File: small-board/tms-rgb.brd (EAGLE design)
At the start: 53.1 x 17.6 mm, 38 parts, among them J1 Pads, U1 CD74HC4053PWR, U100 TMS992XA, U2 LM1881MX/NOPB, U3 MAX4395EUD, U4 TS5A4597DCKR, U5 SN74LVC2G17DCKR, U6 LMH1251MT/NOPB, U7 THS7374IPWR

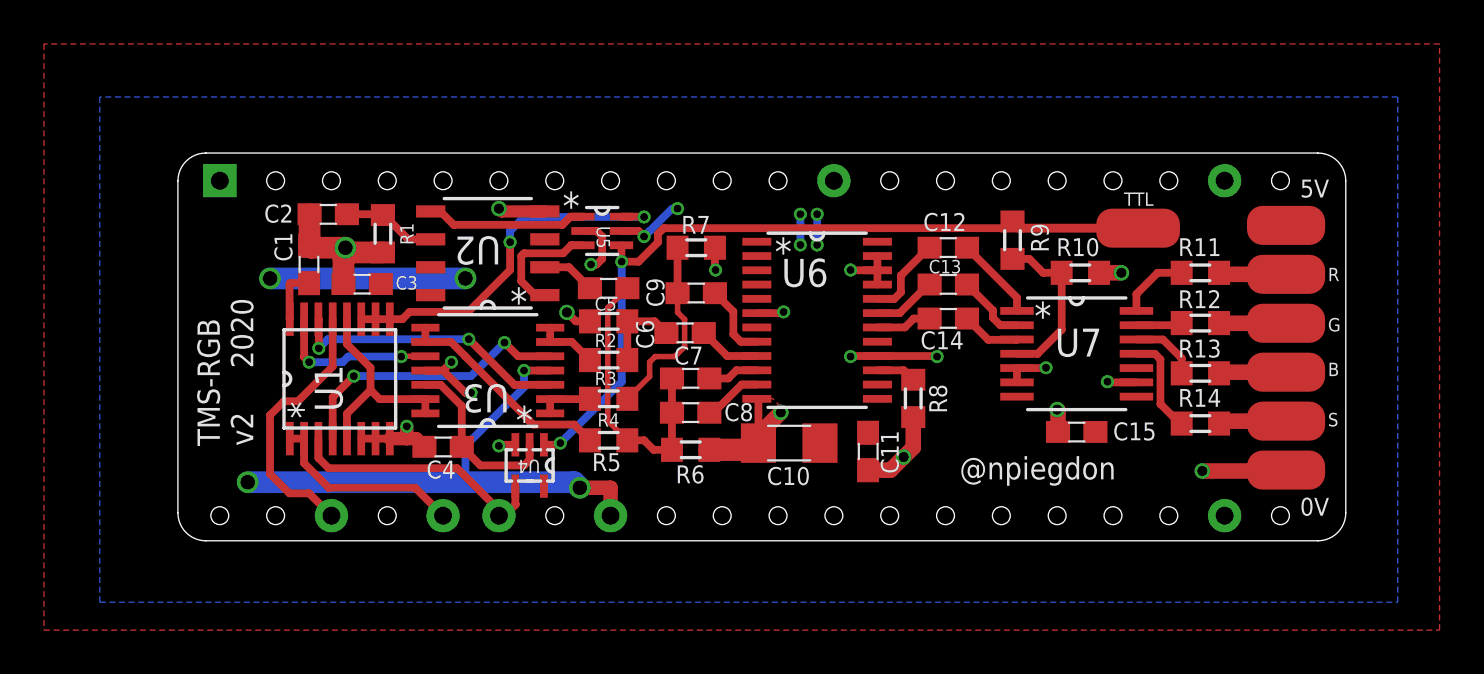
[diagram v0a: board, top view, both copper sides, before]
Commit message: More than 100 improvements
Nearly all of which were suggested by MrPix from the AtariAge forums to improve the electrical characteristics of the board.
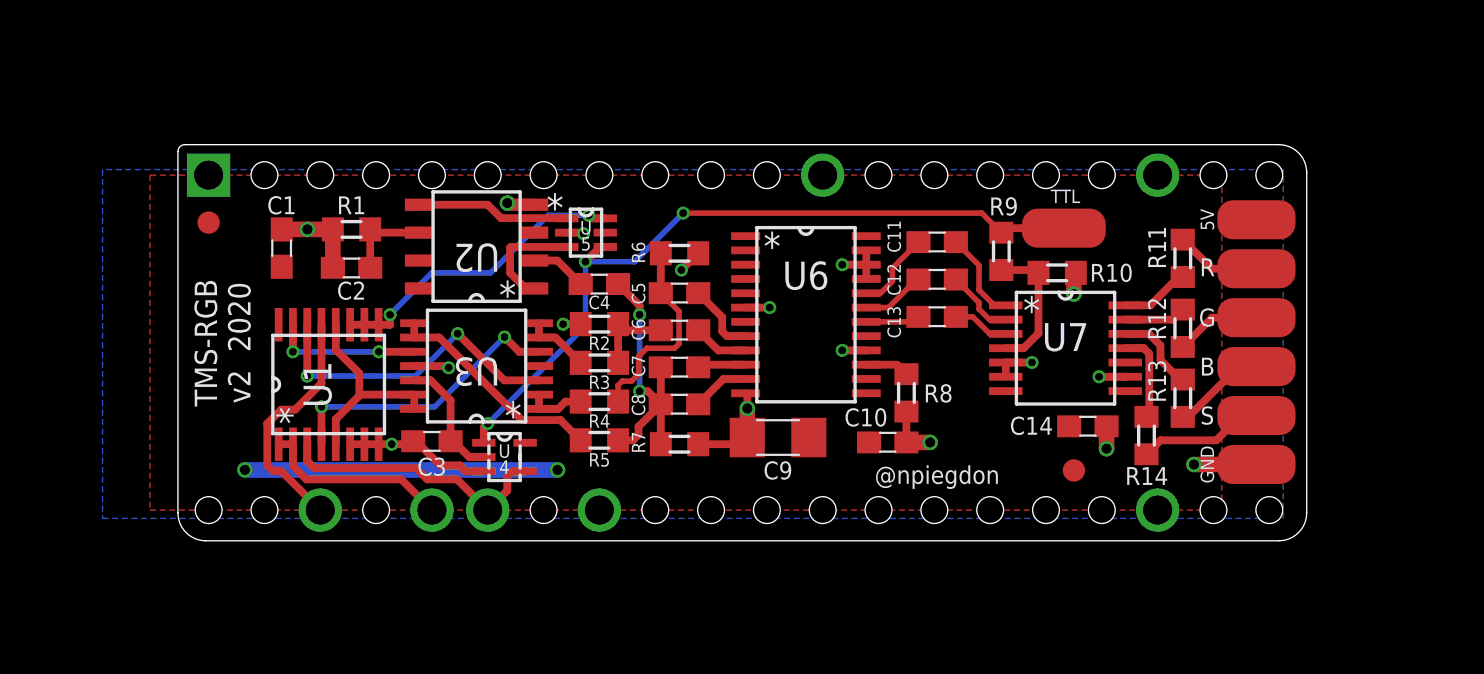
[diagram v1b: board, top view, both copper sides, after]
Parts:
- removed C15: 100nF, tms-rgb:C0603
- added FID1, FID2: FIDUCIAL, tms-rgb:FIDUCIAL
- C10: value 10uF -> 100nF; device tms-rgb:C1206 -> tms-rgb:C0603
- C3: value 100nF -> 10nF
- C4: value 10nF -> 100nF
- C9: value 100nF -> 10uF; device tms-rgb:C0603 -> tms-rgb:C1206
- moved C4 10.3 mm to (19.2, 11.7)
- moved C11 10.0 mm to (34.5, 13.6), turned to 0 degrees
- moved R7 8.97 mm to (22.8, 4.39)
- moved R6 8.96 mm to (22.8, 13.1)
- moved C14 8.02 mm to (41.4, 5.21)
- moved C3 7.83 mm to (11.6, 4.53)
- moved C9 7.55 mm to (27.3, 4.70), turned to 180 degrees
- moved C10 4.48 mm to (32.3, 4.48), turned to 0 degrees
- moved C5 3.23 mm to (22.8, 11.3), turned to 0 degrees
- moved C2 2.66 mm to (7.90, 12.4)
- moved R14 2.51 mm to (44.1, 4.79), turned to 270 degrees
- moved C13 1.56 mm to (34.5, 10.2)
- moved C12 1.53 mm to (34.5, 11.9)
- moved C1 1.45 mm to (4.72, 13.3)
- moved R1 1.44 mm to (7.90, 14.2), turned to 0 degrees
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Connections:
- net GND: now also C14.2, C9.2; no longer C11.2, C15.2, C4.2
- net HOLD: now also C3.1; no longer C4.1
- net N$20: now also C4.2; no longer C5.2
- net N$21: now also C5.2; no longer C9.2
- net N$25: now also C11.1; no longer C12.1
- net N$26: now also C12.1; no longer C13.1
- net N$27: now also C13.1; no longer C14.1
- net N$28: now also C11.2; no longer C12.2
- net N$29: now also C12.2; no longer C13.2
- net N$30: now also C13.2; no longer C14.2
- net SC_R: now also C5.1, R6.2; no longer C9.1, R7.2
- net SC_Y: now also C4.1, R7.2; no longer C5.1, R6.2
- net VCC: now also C14.1, C9.1; no longer C11.1, C15.1, C3.1
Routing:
- net VCC: track 42.6 -> 14.2 mm, vias 11 -> 2
- net GND: track 47.9 -> 36.1 mm, vias 20 -> 17
- net BURST: track 16.9 -> 14.0 mm
- net S75: track 3.09 -> 5.81 mm
- net HOLD: track 8.14 -> 5.70 mm
- net MX_R: track 12.9 -> 14.6 mm
- net N$16: track 7.58 -> 6.26 mm
- net B: track 3.07 -> 4.30 mm
- net R-Y: track 12.2 -> 11.1 mm
- net CSYNC: track 35.5 -> 34.5 mm, vias 2 -> 3
- net G: track 3.05 -> 3.90 mm
- net R: track 3.08 -> 3.90 mm
- net N$17: track 3.10 -> 3.86 mm
- net N$18: track 2.10 -> 2.81 mm
- net MX_Y: track 7.45 -> 6.75 mm
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- removed copper zone on layer 1, net GND
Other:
- board size 53.1 x 17.6 mm -> 51.4 x 18 mm
- board text added: "GND"
- board text added: "U 4"
- board text added: "U 5"
- board text removed: "0V"

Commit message: Updated voltage dividers
Now we consume around 15mA less with no discernible change to the image.
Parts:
- R4: value 220 -> 910
- R5: value 27 -> 160
- R6: value 150 -> 620
- R7: value 150 -> 910
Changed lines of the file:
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@@
 <attribute name="NAME" x="33.9314375" y="6.2992" size="0.8128" layer="25"/>
 </element>
-<element name="R4" library="tms-rgb" package="R0603" value="220" x="19.177" y="6.334125" smashed="yes">
+<element name="R4" library="tms-rgb" package="R0603" value="910" x="19.177" y="6.334125" smashed="yes">
 <attribute name="NAME" x="19.177" y="5.1435" size="0.6096" layer="25" align="bottom-center"/>
 </element>
@@
 <attribute name="NAME" x="19.177" y="6.9088" size="0.6096" layer="25" align="bottom-center"/>
 </element>
-<element name="R5" library="tms-rgb" package="R0603" value="27" x="19.177" y="4.572" smashed="yes">
+<element name="R5" library="tms-rgb" package="R0603" value="160" x="19.177" y="4.572" smashed="yes">
 <attribute name="NAME" x="19.177" y="3.3782" size="0.6096" layer="25" align="bottom-center"/>
 </element>
-<element name="R6" library="tms-rgb" package="R0603" value="150" x="22.821" y="13.080996875" smashed="yes" rot="R180">
+<element name="R6" library="tms-rgb" package="R0603" value="620" x="22.821" y="13.080996875" smashed="yes" rot="R180">
 <attribute name="NAME" x="21.2598" y="12.612" size="0.6096" layer="25" rot="R90"/>
 </element>
@@
 <attribute name="NAME" x="19.177" y="8.683625" size="0.6096" layer="25" align="bottom-center"/>
 </element>
-<element name="R7" library="tms-rgb" package="R0603" value="150" x="22.821" y="4.3942" smashed="yes" rot="R180">
+<element name="R7" library="tms-rgb" package="R0603" value="910" x="22.821" y="4.3942" smashed="yes" rot="R180">
 <attribute name="NAME" x="21.2598" y="3.976" size="0.6096" layer="25" rot="R90"/>
 </element>

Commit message: Updated instructions URL
The new place is https://tms-rgb.com
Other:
- board text added: "For installation instructions, visit: https://tms-rgb.com"
- board text removed: "For installation instructions, visit: https://nicholas.piegdon.info/tms-rgb"
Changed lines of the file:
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@@
 v2  2020</text>
 <text x="34.544" y="2.5908" size="0.8128" layer="25" rot="R180" align="top-center">@npiegdon</text>
-<text x="50.419" y="5.1308" size="1.27" layer="22" rot="MR0">For installation instructions, visit:
-https://nicholas.piegdon.info/tms-rgb</text>
+<text x="48.895" y="9.1948" size="1.27" layer="22" rot="MR0">For installation instructions, visit:
+https://tms-rgb.com</text>
 <text x="18.5674" y="13.208" size="0.6096" layer="25" distance="20" align="bottom-center">U
 5</text>
